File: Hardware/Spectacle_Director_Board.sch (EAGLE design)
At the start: 69 parts, among them J1 AUDIO-JACK3, J4 AUDIO-JACK3, Q2 MBT3904DW1T1, U1 CY7C65213, U2 ESP3212, U3 AP2112K-3.3V, U5 W25Q32FVSS, Y1 26MHz, Y2 32.768kHz

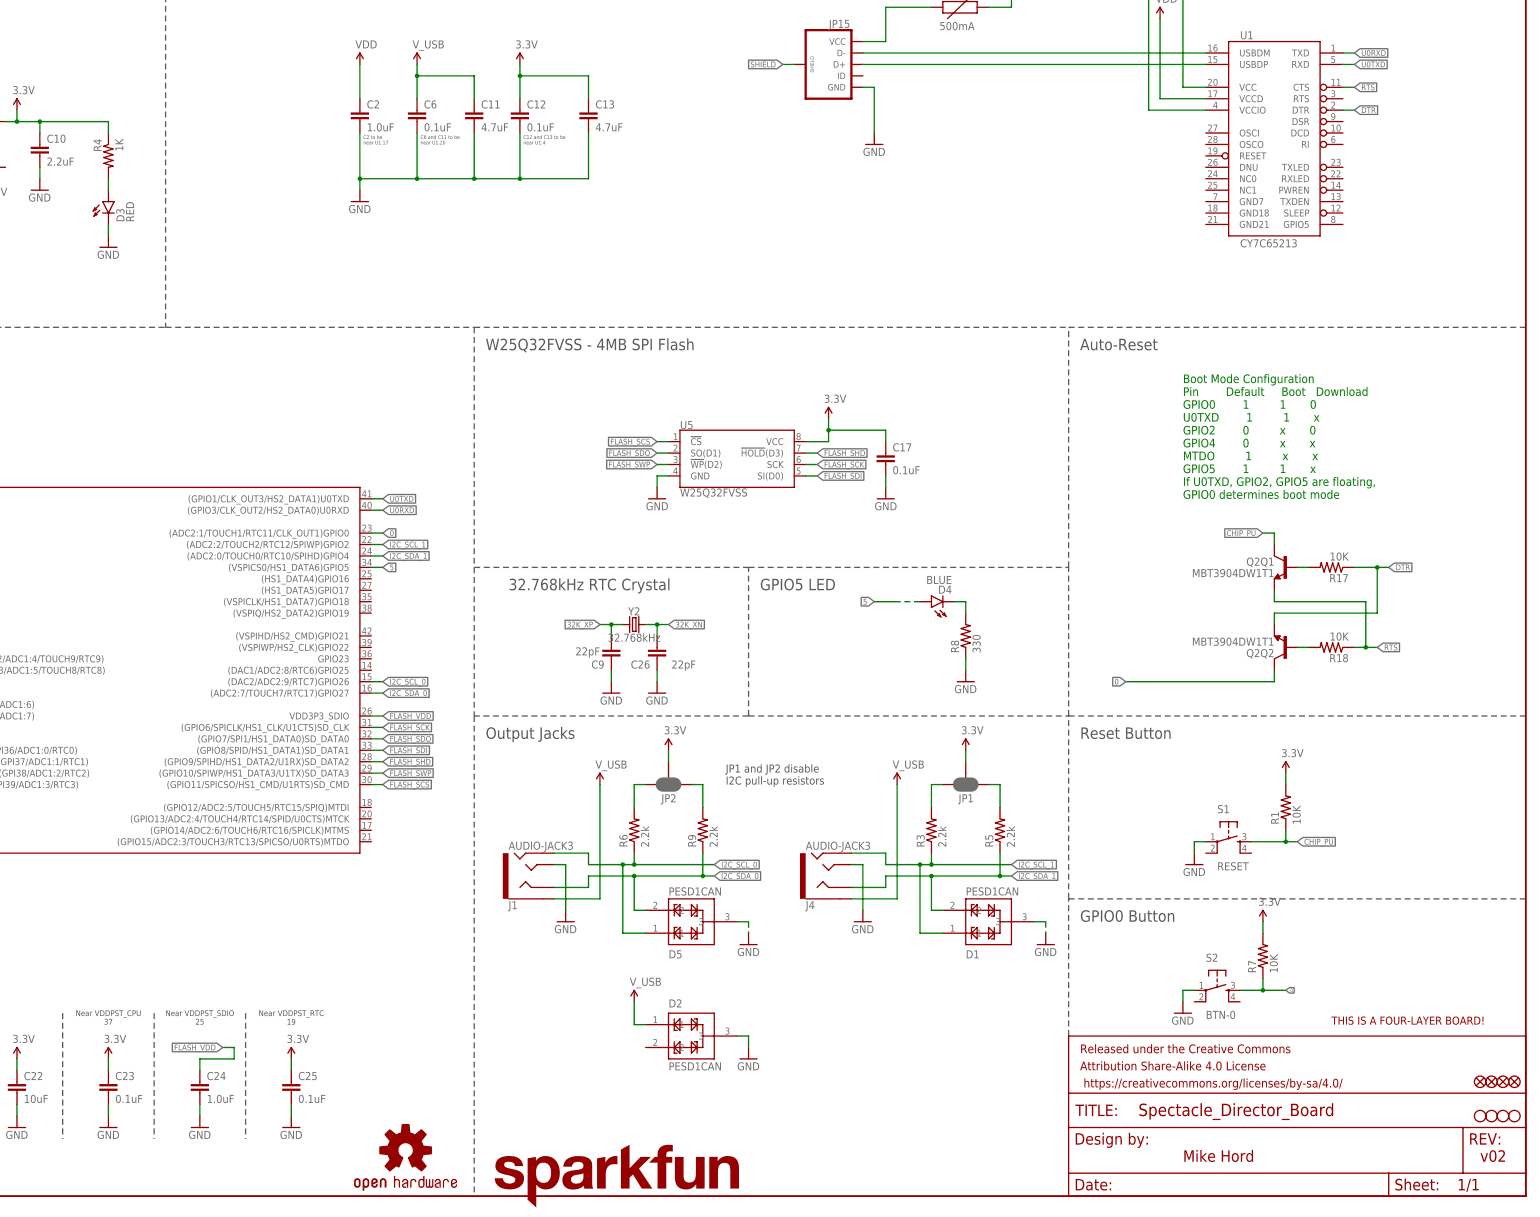
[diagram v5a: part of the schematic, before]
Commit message: v03 - Removing RTC, I2C connector A, adding button, LED.
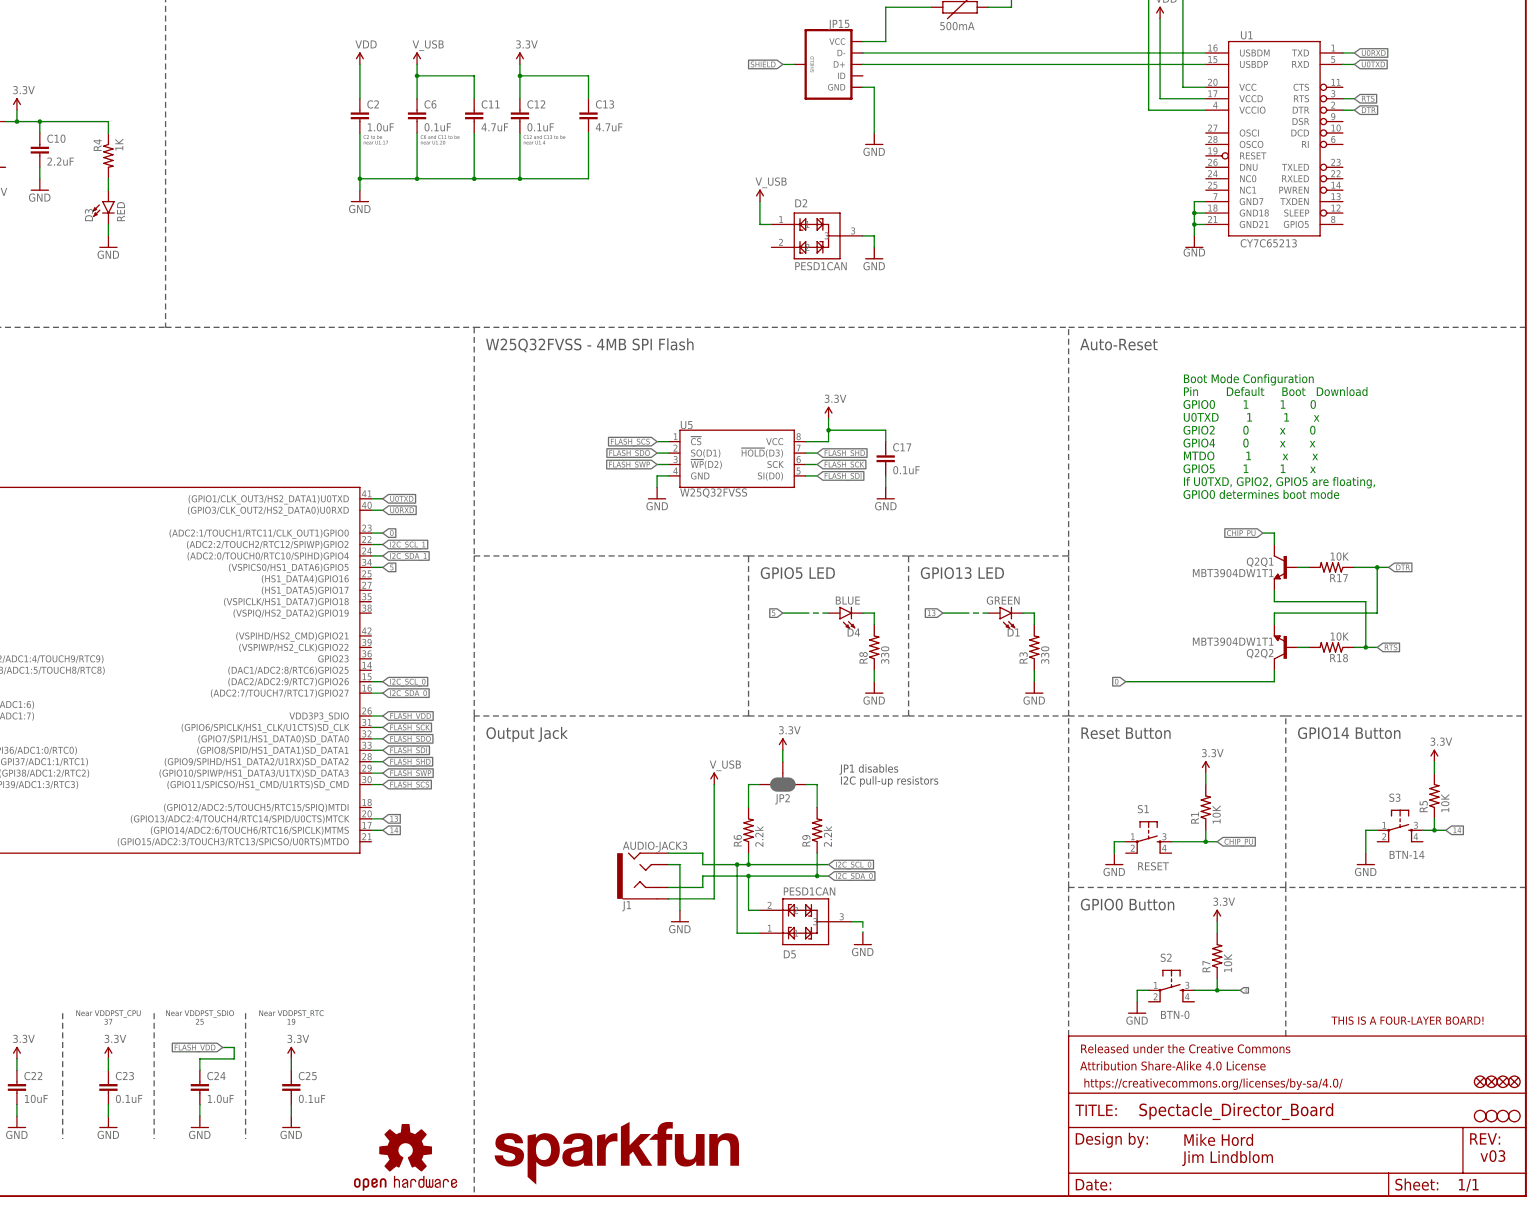
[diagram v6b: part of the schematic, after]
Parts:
- removed C26, C9: 22pF, SparkFun-Capacitors:22PF-50V-5%(0603)
- removed J4: AUDIO-JACK3, SparkFun-Connectors:AUDIO-JACK3
- removed JP1: JUMPER-PAD-3-NC_BY_PASTE, SparkFun-Passives:JUMPER-PAD-3-NC_BY_PASTE
- removed Y2: 32.768kHz, SparkFun-Clocks:CRYSTAL-32.768KHZSMD-3.2X1.5
- added S3: BTN-14, SparkFun-Electromechanical:SWITCH_SPST_4_PINRECT
- D1: value PESD1CAN -> GREEN; device SparkFun-DiscreteSemi:PESD1CAN -> SparkFun-LED:LED-GREEN0603
- R3: value 2.2k -> 330; device SparkFun-Resistors:2.2KOHM-1/10W-1%(0603) -> SparkFun-Resistors:330OHM1/10W1%(0603)
- R5: value 2.2k -> 10K; device SparkFun-Resistors:2.2KOHM-1/10W-1%(0603) -> SparkFun-Resistors:10KOHM-1/10W-1%(0603)0603
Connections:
- removed net N$6: JP1.1, R5.2
- new net 13: D1.A, U2.(GPIO13/ADC2:4/TOUCH4/RTC14/SPID/U0CTS)MTCK
- new net 14: R5.1, S3.3, U2.(GPIO14/ADC2:6/TOUCH6/RTC16/SPICLK)MTMS
- net 3.3V: now also R5.2; no longer JP1.2
- net 32K_XN: no longer C26.2, Y2.2
- net 32K_XP: no longer C9.2, Y2.1
- net GND: now also R3.1, S3.1, U1.GND18, U1.GND21, U1.GND7; no longer C26.1, C9.1, D1.3, J4.TIP
- net I2C_SCL_1: no longer D1.1, J4.RING2, R3.1
- net I2C_SDA_1: no longer D1.2, J4.RING1, R5.1
- net N$3: now also D1.C; no longer JP1.3
- net RTS: now also U1.RTS; no longer U1.CTS
- net V_USB: no longer J4.EARTH
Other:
- note added: "GPIO13 LED"
- note added: "GPIO14 Button"
- note added: "JP1 disables I2C pull-up resistors"
- note added: "Mike Hord Jim Lindblom"
- note added: "Output Jack"
- note added: "v03"
- note removed: "32.768kHz RTC Crystal"
- note removed: "JP1 and JP2 disable I2C pull-up resistors"
- note removed: "Mike Hord"
- note removed: "Output Jacks"
- note removed: "v02"
- moved on the sheet: D2, D5, J1, JP2, R1, R3, R5, R6, R7, R8, R9, S1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

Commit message: initial commit of SAMD21-based director board.
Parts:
- removed C13: 4.7uF, SparkFun-Capacitors:4.7UF-16V-20%,+80%-(1206)
- removed C14, C24: 1.0uF, SparkFun-Capacitors:1.0UF-16V-10%(0603)
- removed C17: 0.1uF, SparkFun-Capacitors:0.1UF-25V(+80/-20%)(0603)
- removed C18, C20, C21, C23, C25: 0.1uF, SparkFun-Capacitors:0.1UF-16V(+-10%)(0402)
- removed C22: 10uF, SparkFun-Capacitors:10UF-6.3V-20%(0603)
- removed C3, C4: 10pF, SparkFun-Capacitors:10PF-50V-5%(0603)
- removed C5: 10nF, SparkFun-Capacitors:10NF/10000PF-50V-10%(0603)
- removed D4: BLUE, SparkFun-LED:LED-BLUE0603
- removed E1: ANTENNA, esp32-thing-temp:ANTENNATRACE-TUNED
- removed FD3, FD4: FIDUCIALUFIDUCIAL, SparkFun-Aesthetics:FIDUCIALUFIDUCIAL
- removed FRAME1: FRAME-LEDGER, SparkFun-Aesthetics:FRAME-LEDGER
- removed L2: DNP, SparkFun-Passives:INDUCTOR0603
- removed R17, R18: 10K, SparkFun-Resistors:10KOHM1/10W1%(0603)0603
- removed R3: 330, SparkFun-Resistors:330OHM1/10W1%(0603)
- removed U$2: FOUR_LAYER_WARNING, SparkFun-Aesthetics:FOUR_LAYER_WARNING
- removed U1: CY7C65213, SparkFun-DigitalIC:CY7C65213
- removed U2: ESP3212, esp32-thing-temp:ESP3212
- removed Y1: 26MHz, things:CRYSTAL-GROUNDED3.2X2.5
- added D7: BLUE, SparkFun-LED:LED-BLUE0603
- added D8: GREEN, SparkFun-LED:LED-GREEN0603
- added D9: Yellow, SparkFun-LED:LED-YELLOW0603
- added FRAME2: FRAME-LETTER, SparkFun-Aesthetics:FRAME-LETTER
- added J2: CORTEX_DEBUGPTH, SparkFun-Connectors:CORTEX_DEBUGPTH
- added LOGO3: SFE_LOGO_FLAME.2EXP, SparkFun-Aesthetics:SFE_LOGO_FLAME.2EXP
- added Q1: 2N7002PW, SparkFun-DiscreteSemi:MOSFET-NCHANNEL2N7002PW
- added R10, R12, R13: 330, SparkFun-Resistors:330OHM1/10W1%(0603)
- added R15: 100k, SparkFun-Resistors:100KOHM-1/10W-1%(0603)
- added TP1, TP2, TP3, TP4, TP5: TEST-POINT3X5, SparkFun-Connectors:TEST-POINT3X5
- added U4: ATSAMD21G-A, samd21-temp:ATSAMD21G-A
- C1: value 3.0nF -> 0.1uF; device esp32-thing-temp:3.0NF-0603-50V-5% -> SparkFun-Capacitors:0.1UF-25V(+80/-20%)(0603)
- C11: value 4.7uF -> 0.1uF; device SparkFun-Capacitors:4.7UF-16V-20%,+80%-(1206) -> SparkFun-Capacitors:0.1UF-25V(+80/-20%)(0603)
- C12, C6: device SparkFun-Capacitors:0.1UF-25V-5%(0603) -> SparkFun-Capacitors:0.1UF-25V(+80/-20%)(0603)
- C2: value 1.0uF -> 0.1uF; device SparkFun-Capacitors:1.0UF-16V-10%(0603) -> SparkFun-Capacitors:0.1UF-25V(+80/-20%)(0603)
- C8: value 5.6pF -> 0.1uF; device SparkFun-Capacitors:CAP0603-CAP -> SparkFun-Capacitors:0.1UF-25V(+80/-20%)(0603); PROD_ID CAP-12456 -> (none)
- JP2: value JUMPER-PAD-3-NC_BY_PASTE -> JUMPER-SMT_3_2-NC_TRACE_SILK; device SparkFun-Passives:JUMPER-PAD-3-NC_BY_PASTE -> SparkFun-Jumpers:JUMPER-SMT_3_2-NC_TRACE_SILK
- L1: value DNP -> FB - 30Ohm; PROD_ID (none) -> RES-07859
- Q2: value MBT3904DW1T1 -> 2N7002PW; device esp32-thing-temp:MBT3904DW1T1 -> SparkFun-DiscreteSemi:MOSFET-NCHANNEL2N7002PW
- R2: value 20k -> 330; device SparkFun-Resistors:20KOHM1/10W1%(0603) -> SparkFun-Resistors:330OHM1/10W1%(0603)
- R8: value 330 -> 100k; device SparkFun-Resistors:330OHM1/10W1%(0603) -> SparkFun-Resistors:100KOHM-1/10W-1%(0603)
- S2: value BTN-0 -> BTN2
- S3: value BTN-14 -> BTN1
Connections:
- removed net 0: Q2Q2.C, R7.1, S2.3, U2.(ADC2:1/TOUCH1/RTC11/CLK_OUT1)GPIO0
- removed net 13: D1.A, U2.(GPIO13/ADC2:4/TOUCH4/RTC14/SPID/U0CTS)MTCK
- removed net 14: R5.1, S3.3, U2.(GPIO14/ADC2:6/TOUCH6/RTC16/SPICLK)MTMS
- removed net 32K_XN: U2.32K_XN(GPIO33/ADC1:5/TOUCH8/RTC8)
- removed net 32K_XP: U2.32K_XP(GPIO32/ADC1:4/TOUCH9/RTC9)
- removed net 5: D4.A, U2.(VSPICS0/HS1_DATA6)GPIO5
- removed net CAP_10N: C1.1, C5.2, R2.1, U2.CAP1
- removed net CHIP_PU: Q2Q1.C, R1.1, S1.3, U2.CHIP_PU
- removed net DTR: Q2Q2.E, R17.1, U1.DTR
- removed net FLASH_SCK: U2.(GPIO6/SPICLK/HS1_CLK/U1CTS)SD_CLK, U5.SCK
- removed net FLASH_SCS: U2.(GPIO11/SPICSO/HS1_CMD/U1RTS)SD_CMD, U5.!CS!
- removed net FLASH_SDI: U2.(GPIO8/SPID/HS1_DATA1)SD_DATA1, U5.SI(D0)
- removed net FLASH_SDO: U2.(GPIO7/SPI1/HS1_DATA0)SD_DATA0, U5.SO(D1)
- removed net FLASH_SHD: U2.(GPIO9/SPIHD/HS1_DATA2/U1RX)SD_DATA2, U5.!HOLD!(D3)
- removed net FLASH_SWP: U2.(GPIO10/SPIWP/HS1_DATA3/U1TX)SD_DATA3, U5.!WP!(D2)
- removed net FLASH_VDD: C24.1, U2.VDD3P3_SDIO
- removed net I2C_SCL_0: D5.1, J1.RING2, R6.1, U2.(DAC2/ADC2:9/RTC7)GPIO26
- removed net I2C_SCL_1: U2.(ADC2:2/TOUCH2/RTC12/SPIWP)GPIO2
- removed net I2C_SDA_0: D5.2, J1.RING1, R9.1, U2.(ADC2:7/TOUCH7/RTC17)GPIO27
- removed net I2C_SDA_1: U2.(ADC2:0/TOUCH0/RTC10/SPIHD)GPIO4
- removed net LNA_IN: C8.1, L1.1, U2.LNA_IN
- removed net N$3: D1.C, R3.2
- removed net N$8: JP15.D+, U1.USBDP
- removed net RTS: Q2Q1.E, R18.1, U1.RTS
- removed net TRACE_ANT: C8.2, E1.SIGNAL, L2.1
- removed net U0RXD: U1.TXD, U2.(GPIO3/CLK_OUT2/HS2_DATA0)U0RXD
- removed net U0TXD: U1.RXD, U2.(GPIO1/CLK_OUT3/HS2_DATA1)U0TXD
- removed net VDD: C2.1, U1.VCCD
- removed net XTAL_N_: C4.2, U2.XTAL_N, Y1.2
- removed net XTAL_P_: C3.2, U2.XTAL_P, Y1.1
- new net !RESET: J2.!RESET, R1.1, S1.3, S1.4, TP3.1, U4.!RESET!
- new net A0: U4.PA02(AIN0/DAC)
- new net A1: U4.PB08(AIN2/SER4:0/TC4:0)
- new net A2: U4.PB09(AIN3/SER4:1/TC4:1)
- new net A3: U4.PA04(AIN4/REFB/SER0:0/TC0:0)
- new net A4_FLASH!WP!: U4.PA05(AIN5/SER0:1/TC0:1), U5.!WP!(D2)
- new net A5: U4.PB02(AIN10/SER5:0)
- new net AREF: U4.PA03(AIN1/REFA)
- new net D10: U4.PA18(SER1:2+)
- new net D11: U4.PA16(I2C/SER1:0+)
- new net D12_BTN1: R5.1, S3.3, S3.4, U4.PA19(SER1:3+)
- new net D13_LED1: Q2.G, R15.2, U4.PA17(I2C/SER1:1+)
- new net D2: U4.PA14(XIN/SER2:2+)
- new net D5: U4.PA15(XOUT/SER2:3+)
- new net D6_BTN2: R7.1, S2.3, S2.4, U4.PA20(SER5:2+)
- new net D7_LED2: Q1.G, R8.2, U4.PA21(SER5:3+)
- new net D8_FLASH!CS!: U4.PA06(AIN6/SER0:2/TC1:0), U5.!CS!
- new net D9_FLASH!HD!: U4.PA07(AIN7/SER0:3/TC1:1), U5.!HOLD!(D3)
- new net N$9: D7.A, R10.1
- new net PB22: U4.PB22(SER5:2+)
- new net PB23: U4.PB23(SER5:3+)
- new net RX_LED: D9.C, U4.PB03(AIN11/SER5:1)
- new net SCL: D5.1, J1.RING2, R6.1, U4.PA23(I2C/SER3:0+)
- new net SDA: D5.2, J1.RING1, R9.1, U4.PA22(I2C/SER3:0+)
- new net SPI_MISO: U4.PA12(I2C/SER2:0+), U5.SO(D1)
- new net SPI_MOSI: U4.PB10(SER4:2+), U5.SI(D0)
- new net SPI_SCK: U4.PB11(SER4:3+), U5.SCK
- new net SWCLK: J2.SWDCLK/TCK, TP2.1, U4.PA30(SWCLK/SER1:2+)
- new net SWDIO: J2.SWDIO/TMS, TP1.1, U4.PA31(SWDIO/SER1:3+)
- new net TX_LED: D8.C, U4.PA27
- new net USB_D+: JP15.D+, U4.PA25(SER3:3+)
- new net USB_D-: JP15.D-, U4.PA24(SER3:2+)
- new net USB_HOST_EN: U4.PA28
- new net VDDANA: C6.1, L1.2, U4.VDDANA
- new net VDDCORE: C1.1, U4.VDDCORE
- net 3.3V: now also C11.1, C2.1, C8.1, J2.VCC, L1.1, R10.2, R12.2, R13.2, R2.2, TP4.1, U4.VDDIN, U4.VDDIO@17, U4.VDDIO@36; no longer C13.1, C14.1, C17.1, C18.1, C20.1, C21.1, C22.1, C23.1, C25.1, U1.VCCIO, U2.VDD3P3_CPU, U2.VDD3P3_RTC, U2.VDDA, U2.VDDA3P3
- net GND: now also C1.2, C8.2, J2.GND@3, J2.GND@5, Q1.S, Q2.S, R15.1, S1.2, S2.2, S3.2, TP5.1, U4.GND@18, U4.GND@35, U4.GND@42, U4.GNDANA; no longer C13.2, C14.2, C17.2, C18.2, C20.2, C21.2, C22.2, C23.2, C24.2, C25.2, C3.1, C4.1, C5.1, E1.GND, L1.2, L2.2, R3.1, U1.GND18, U1.GND21, U1.GND7, U2.GND, Y1.GND
- net N$1: now also D1.A, R2.1; no longer D4.C, R8.2
- net N$10: now also D7.C, Q2.D; no longer Q2Q1.B, R17.2
- net N$11: now also D8.A, R12.1; no longer C1.2, R2.2, U2.CAP2
- net N$12: now also D9.A, R13.1; no longer Q2Q2.B, R18.2
- net N$7: now also D1.C, Q1.D; no longer JP15.D-, U1.USBDM
- net V_USB: no longer C11.1, C6.1, U1.VCC
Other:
- note added: "ATSAMD21G18 VDD Range: 1.62-3.63V"
- note added: "v04"
- note removed: "Auto-Reset"
- note removed: "Boot Mode Configuration Pin Default Boot Download GPIO0 1 1 0 U0TXD 1 1 x GPIO2 0 x 0 GPIO4 0 x x MTDO 1 x x GPIO5 1 1 x If U0TXD, GPIO2, GPIO5 are floating, GPIO0 determines boot mode"
- note removed: "C12 and C13 to be near U1.4"
- note removed: "C2 to be near U1.17"
- note removed: "C6 and C11 to be near U1.20"
- note removed: "CY7C65213 (USB-to-Serial Converter)"
- note removed: "Espressif ESP32"
- note removed: "GPIO0 Button"
- note removed: "GPIO13 LED"
- note removed: "GPIO14 Button"
- note removed: "GPIO5 LED"
- note removed: "Near VDDA 46"
- note removed: "Near VDDA3P3 3/4"
- note removed: "Near VDDA_LNA 1"
- note removed: "Near VDDPST_CPU 37"
- note removed: "Near VDDPST_RTC 19"
- note removed: "Near VDDPST_SDIO 25"
- note removed: "Output Jack"
- note removed: "Reset Button"
- note removed: "Voltage Regulator"
- note removed: "W25Q32FVSS - 4MB SPI Flash"
- note removed: "v03"
- moved on the sheet: C1, C10, C11, C12, C2, C6, C7, C8, D2, D5, F1, J1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

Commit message: Cleaning up schematic
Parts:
- TP1: value TEST-POINT3X5 -> TP-SWDIO
- TP2: value TEST-POINT3X5 -> TP-SWCLK
- TP3: value TEST-POINT3X5 -> TP-!RESET!
- TP4: value TEST-POINT3X5 -> TP-3.3V
- TP5: value TEST-POINT3X5 -> TP-GND
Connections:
- removed net A0: U4.PA02(AIN0/DAC)
- removed net A1: U4.PB08(AIN2/SER4:0/TC4:0)
- removed net A2: U4.PB09(AIN3/SER4:1/TC4:1)
- removed net A3: U4.PA04(AIN4/REFB/SER0:0/TC0:0)
- removed net A5: U4.PB02(AIN10/SER5:0)
- removed net AREF: U4.PA03(AIN1/REFA)
- removed net D11: U4.PA16(I2C/SER1:0+)
- removed net D2: U4.PA14(XIN/SER2:2+)
- removed net D5: U4.PA15(XOUT/SER2:3+)
- removed net PB22: U4.PB22(SER5:2+)
- removed net PB23: U4.PB23(SER5:3+)
- removed net USB_HOST_EN: U4.PA28
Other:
- note added: "ATSAMD21G18A"
- note added: "Buttons"
- note added: "Debug/Program Interface"
- note added: "I2C Interface"
- note added: "RX/TX LED's"
- note added: "SPI Flash"
- note added: "UI LED's"
- note added: "USB Input & Voltage Regulator"
- moved on the sheet: D5, J1, J2, JP15, JP2, R6, R9, TP1, TP2, TP3, TP4, TP5
